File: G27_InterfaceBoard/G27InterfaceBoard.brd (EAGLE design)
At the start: 60 x 60 mm, 24 parts, among them IC1 LMV321M5, J1 Pedal, J2 Shifter, J3 Steering, U1 LMV324

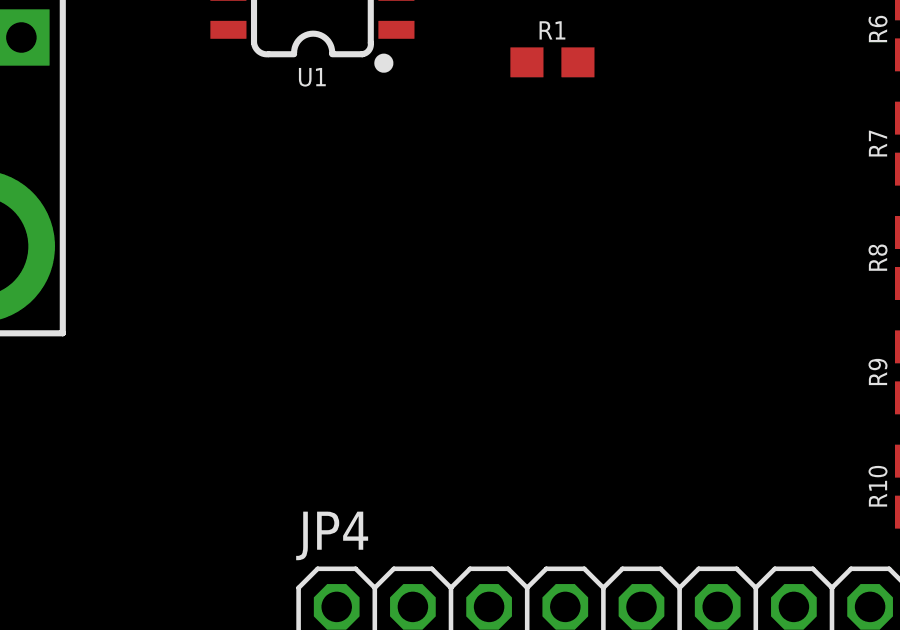
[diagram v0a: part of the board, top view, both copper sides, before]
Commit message: Modfications to board based on testing.
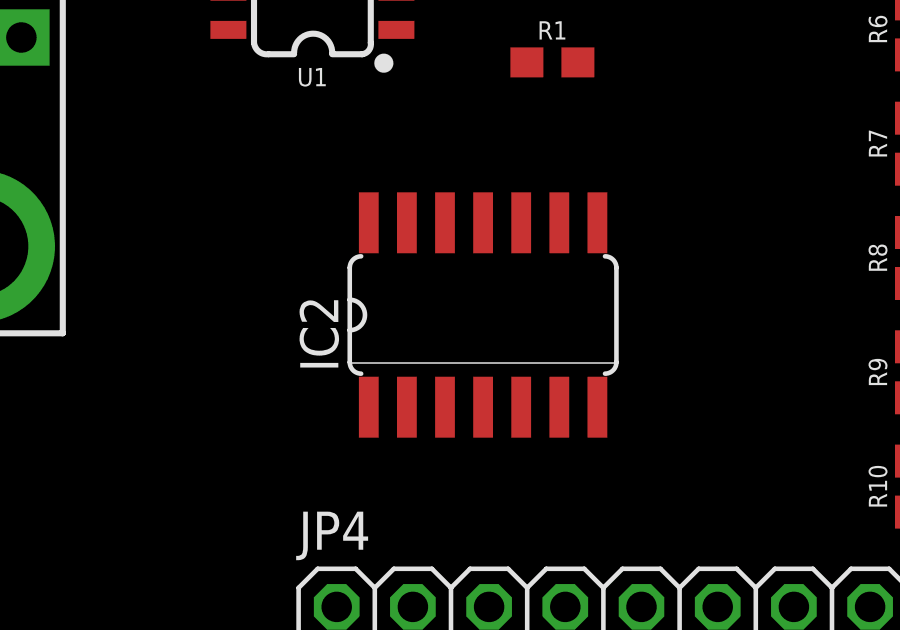
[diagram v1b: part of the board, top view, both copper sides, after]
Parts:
- added IC2: 74HC126D, 74xx-eu:SO14
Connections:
- removed net !SHIFT_CS: J2.3, JP4.17
- removed net !WBTN_CS: JP4.13
- removed net !WLED_CS: JP4.15
- removed net +5V: C1.1, C2.1, D1.3, IC1.5, J1.6, J1.9, J2.7, J2.9, J3.7, JP4.19, U1.4
- removed net N$4: C2.2, IC1.2
- new net !SHIFT_PWR_LED: J2.5
- new net SHIFT_CS: IC2.1, J2.3, JP4.17
- new net SHIFT_MISO: IC2.2, J2.2
- new net VCC: C1.1, C2.1, D1.3, IC1.5, IC2.14, J1.6, J1.9, J2.7, J2.9, J3.7, JP4.19, U1.4
- new net WMISO: IC2.5, J3.2
- net GND: now also C2.2, IC1.2, IC2.10, IC2.12, IC2.13, IC2.7, IC2.9
- net MISO: now also IC2.3, IC2.6; no longer J2.2, J3.2
- net MOSI: no longer J2.5
- net N$3: now also IC1.3; no longer IC1.1
- net SHIFT_Y: now also IC1.1; no longer IC1.3
- net WBTN_CS: now also IC2.4, JP4.13
- net WLED_LATCH: now also JP4.15
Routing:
- added copper zone on layer 1, net VCC
- removed copper zone on layer 1, net +5V
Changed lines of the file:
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@@
 <attribute name="NAME" x="48.325" y="-18.975" size="1.27" layer="25" rot="R180"/>
 <attribute name="POPULARITY" value="3" x="-12" y="35" size="1.778" layer="27" rot="R180" display="off"/>
+<attribute name="SPICEPREFIX" value="D" x="46.42" y="-17.07" size="1.778" layer="27" rot="R180" display="off"/>
 <attribute name="VALUE" x="48.325" y="-13.895" size="1.27" layer="27" rot="R180"/>
 </element>
@@
 <attribute name="VALUE" x="20.31" y="-24.97" size="0.6096" layer="27" font="vector" ratio="20" rot="R180" align="bottom-center"/>
 </element>
+<element name="IC2" library="74xx-eu" library_urn="urn:adsk.eagle:library:85" package="SO14" package3d_urn="urn:adsk.eagle:package:1010/2" value="74HC126D" x="26" y="-44" smashed="yes">
+<attribute name="NAME" x="21.174" y="-45.905" size="1.27" layer="25" ratio="10" rot="R90"/>
+<attribute name="POPULARITY" value="0" x="26" y="-44" size="1.778" layer="27" display="off"/>
+<attribute name="VALUE" x="22.825" y="-44.762" size="1.27" layer="27" ratio="10"/>
+</element>
 </elements>
 <signals>
-<signal name="+5V">
-<contactref element="J2" pad="7"/>
-<contactref element="J2" pad="9"/>
-<contactref element="JP4" pad="19"/>
-<contactref element="U1" pad="4"/>
-<contactref element="C1" pad="1"/>
-<contactref element="D1" pad="3"/>
-<contactref element="J1" pad="6"/>
-<contactref element="J1" pad="9"/>
-<contactref element="J3" pad="7"/>
-<contactref element="IC1" pad="5"/>
-<contactref element="C2" pad="1"/>
-<polygon width="0.1524" layer="1">
-<vertex x="-3" y="2"/>
-<vertex x="61" y="2"/>
-<vertex x="61" y="-62"/>
-<vertex x="-3" y="-62"/>
-</polygon>
-</signal>
 <signal name="THROTTLE">
 <contactref element="J1" pad="2"/>
@@
 <vertex x="-3" y="-61"/>
 </polygon>
-<wire x1="10.61" y1="-34.75" x2="17.51" y2="-30.685" width="0" layer="19" extent="1-1"/>
-<wire x1="40.23" y1="-50.57" x2="43.98" y2="-53.73" width="0" layer="19" extent="1-1"/>
-<wire x1="40.23" y1="-42.95" x2="45.31" y2="-47.18" width="0" layer="19" extent="1-1"/>
-<wire x1="40.23" y1="-35.33" x2="40.23" y2="-42.95" width="0" layer="19" extent="1-1"/>
-<wire x1="40.23" y1="-31.52" x2="40.23" y2="-35.33" width="0" layer="19" extent="1-1"/>
-<wire x1="40.23" y1="-27.71" x2="40.23" y2="-31.52" width="0" layer="19" extent="1-1"/>
+<contactref element="IC2" pad="7"/>
+<contactref element="IC1" pad="2"/>
+<contactref element="C2" pad="2"/>
+<contactref element="IC2" pad="12"/>
+<contactref element="IC2" pad="9"/>
+<contactref element="IC2" pad="10"/>
+<contactref element="IC2" pad="13"/>
+<wire x1="28.54" y1="-40.9266" x2="29.81" y2="-47.0734" width="0" layer="19" extent="1-1"/>
+<wire x1="27.27" y1="-40.9266" x2="28.54" y2="-40.9266" width="0" layer="19" extent="1-1"/>
+<wire x1="24.73" y1="-40.9266" x2="27.27" y2="-40.9266" width="0" layer="19" extent="1-1"/>
+<wire x1="23.46" y1="-40.9266" x2="24.73" y2="-40.9266" width="0" layer="19" extent="1-1"/>
+<wire x1="10.61" y1="-34.75" x2="28.54" y2="-40.9266" width="0" layer="19" extent="1-1"/>
+<wire x1="17.51" y1="-30.685" x2="10.61" y2="-34.75" width="0" layer="19" extent="1-1"/>
 <wire x1="27.32" y1="-30.58" x2="17.51" y2="-30.685" width="0" layer="19" extent="1-1"/>
+<wire x1="30.97" y1="-22.58" x2="27.32" y2="-30.58" width="0" layer="19" extent="1-1"/>
+<wire x1="24.47" y1="-19.446" x2="30.97" y2="-22.58" width="0" layer="19" extent="1-1"/>
+<wire x1="40.23" y1="-27.71" x2="30.97" y2="-22.58" width="0" layer="19" extent="1-1"/>
+<wire x1="40.23" y1="-31.52" x2="40.23" y2="-27.71" width="0" layer="19" extent="1-1"/>
+<wire x1="40.23" y1="-35.33" x2="40.23" y2="-31.52" width="0" layer="19" extent="1-1"/>
+<wire x1="40.23" y1="-42.95" x2="40.23" y2="-35.33" width="0" layer="19" extent="1-1"/>
+<wire x1="45.31" y1="-47.18" x2="40.23" y2="-42.95" width="0" layer="19" extent="1-1"/>
+<wire x1="40.23" y1="-50.57" x2="45.31" y2="-47.18" width="0" layer="19" extent="1-1"/>
+<wire x1="43.98" y1="-53.73" x2="40.23" y2="-50.57" width="0" layer="19" extent="1-1"/>
+<wire x1="34.94" y1="-7.72" x2="30.97" y2="-22.58" width="0" layer="19" extent="1-1"/>
 </signal>
 <signal name="SCK">
@@
 </signal>
 <signal name="MISO">
-<contactref element="J2" pad="2"/>
 <contactref element="JP4" pad="16"/>
-<contactref element="J3" pad="2"/>
-<wire x1="45.31" y1="-44.64" x2="33.56" y2="-10.56" width="0" layer="19" extent="1-1"/>
-<wire x1="38.9" y1="-53.73" x2="45.31" y2="-44.64" width="0" layer="19" extent="1-1"/>
-</signal>
-<signal name="!SHIFT_CS">
+<contactref element="IC2" pad="3"/>
+<contactref element="IC2" pad="6"/>
+<wire x1="28.54" y1="-47.0734" x2="24.73" y2="-47.0734" width="0" layer="19" extent="1-1"/>
+<wire x1="38.9" y1="-53.73" x2="28.54" y2="-47.0734" width="0" layer="19" extent="1-1"/>
+</signal>
+<signal name="SHIFT_CS">
 <contactref element="J2" pad="3"/>
 <contactref element="JP4" pad="17"/>
-<wire x1="41.44" y1="-56.27" x2="30.79" y2="-10.56" width="0" layer="19" extent="1-1"/>
+<contactref element="IC2" pad="1"/>
+<wire x1="41.44" y1="-56.27" x2="22.19" y2="-47.0734" width="0" layer="19" extent="1-1"/>
+<wire x1="30.79" y1="-10.56" x2="41.44" y2="-56.27" width="0" layer="19" extent="1-1"/>
 </signal>
 <signal name="SHIFT_X">
@@
 </signal>
 <signal name="MOSI">
-<contactref element="J2" pad="5"/>
 <contactref element="JP4" pad="14"/>
 <contactref element="J3" pad="3"/>
 <wire x1="45.31" y1="-42.1" x2="36.36" y2="-53.73" width="0" layer="19" extent="1-1"/>
-<wire x1="25.25" y1="-10.56" x2="45.31" y2="-42.1" width="0" layer="19" extent="1-1"/>
 </signal>
 <signal name="SHIFT_Y">
 <contactref element="J2" pad="8"/>
-<contactref element="IC1" pad="3"/>
-<wire x1="25.42" y1="-19.446" x2="29.41" y2="-7.72" width="0" layer="19" extent="1-1"/>
-</signal>
-<signal name="!WLED_CS">
-<contactref element="JP4" pad="15"/>
-</signal>
-<signal name="!WBTN_CS">
-<contactref element="JP4" pad="13"/>
+<contactref element="IC1" pad="1"/>
+<wire x1="23.52" y1="-19.446" x2="29.41" y2="-7.72" width="0" layer="19" extent="1-1"/>
 </signal>
 <signal name="N$1">
@@
 <signal name="WLED_LATCH">
 <contactref element="J3" pad="5"/>
+<contactref element="JP4" pad="15"/>
+<wire x1="45.31" y1="-37.02" x2="38.9" y2="-56.27" width="0" layer="19" extent="1-1"/>
 </signal>
 <signal name="WBTN_CS">
 <contactref element="J3" pad="6"/>
+<contactref element="JP4" pad="13"/>
+<contactref element="IC2" pad="4"/>
+<wire x1="36.36" y1="-56.27" x2="26" y2="-47.0734" width="0" layer="19" extent="1-1"/>
+<wire x1="45.31" y1="-34.48" x2="36.36" y2="-56.27" width="0" layer="19" extent="1-1"/>
 </signal>
 <signal name="N$2">
@@
 <wire x1="40.23" y1="-41.25" x2="40.23" y2="-37.44" width="0" layer="19" extent="1-1"/>
 </signal>
-<signal name="N$4">
-<contactref element="IC1" pad="2"/>
-<contactref element="C2" pad="2"/>
-<wire x1="24.47" y1="-19.446" x2="30.97" y2="-22.58" width="0" layer="19" extent="1-1"/>
-</signal>
 <signal name="N$3">
-<contactref element="IC1" pad="1"/>
 <contactref element="IC1" pad="4"/>
 <contactref element="R9" pad="1"/>
-<wire x1="23.52" y1="-19.446" x2="25.42" y2="-16.834" width="0" layer="19" extent="1-1"/>
-<wire x1="40.23" y1="-46.76" x2="23.52" y2="-19.446" width="0" layer="19" extent="1-1"/>
+<contactref element="IC1" pad="3"/>
+<wire x1="25.42" y1="-19.446" x2="25.42" y2="-16.834" width="0" layer="19" extent="1-1"/>
+<wire x1="40.23" y1="-46.76" x2="25.42" y2="-19.446" width="0" layer="19" extent="1-1"/>
 </signal>
 <signal name="SHIFT_Y_3_3">
@@
 <wire x1="40.23" y1="-48.87" x2="40.23" y2="-45.06" width="0" layer="19" extent="1-1"/>
 </signal>
+<signal name="!SHIFT_PWR_LED">
+<contactref element="J2" pad="5"/>
+</signal>
+<signal name="VCC">
+<contactref element="IC2" pad="14"/>
+<contactref element="JP4" pad="19"/>
+<contactref element="J2" pad="7"/>
+<contactref element="J2" pad="9"/>
+<contactref element="U1" pad="4"/>
+<contactref element="C1" pad="1"/>
+<contactref element="D1" pad="3"/>
+<contactref element="J1" pad="6"/>
+<contactref element="J1" pad="9"/>
+<contactref element="J3" pad="7"/>
+<contactref element="IC1" pad="5"/>
+<contactref element="C2" pad="1"/>
+<polygon width="0.1524" layer="1">
+<vertex x="-3" y="2"/>
+<vertex x="61" y="2"/>
+<vertex x="61" y="-62"/>
+<vertex x="-3" y="-62"/>
+</polygon>
+<wire x1="7.77" y1="-33.36" x2="22.19" y2="-40.9266" width="0" layer="19" extent="1-1"/>
+<wire x1="7.77" y1="-25.06" x2="7.77" y2="-33.36" width="0" layer="19" extent="1-1"/>
+<wire x1="23.11" y1="-30.685" x2="7.77" y2="-33.36" width="0" layer="19" extent="1-1"/>
+<wire x1="25.62" y1="-30.58" x2="23.11" y2="-30.685" width="0" layer="19" extent="1-1"/>
+<wire x1="29.27" y1="-22.58" x2="25.62" y2="-30.58" width="0" layer="19" extent="1-1"/>
+<wire x1="23.52" y1="-16.834" x2="29.27" y2="-22.58" width="0" layer="19" extent="1-1"/>
+<wire x1="26.64" y1="-7.72" x2="23.52" y2="-16.834" width="0" layer="19" extent="1-1"/>
+<wire x1="32.17" y1="-7.72" x2="26.64" y2="-7.72" width="0" layer="19" extent="1-1"/>
+<wire x1="46.42" y1="-18.17" x2="32.17" y2="-7.72" width="0" layer="19" extent="1-1"/>
+<wire x1="45.31" y1="-31.94" x2="46.42" y2="-18.17" width="0" layer="19" extent="1-1"/>
+<wire x1="43.98" y1="-56.27" x2="45.31" y2="-31.94" width="0" layer="19" extent="1-1"/>
+</signal>
+<signal name="WMISO">
+<contactref element="J3" pad="2"/>
+<contactref element="IC2" pad="5"/>
+<wire x1="45.31" y1="-44.64" x2="27.27" y2="-47.0734" width="0" layer="19" extent="1-1"/>
+</signal>
+<signal name="SHIFT_MISO">
+<contactref element="J2" pad="2"/>
+<contactref element="IC2" pad="2"/>
+<wire x1="33.56" y1="-10.56" x2="23.46" y2="-47.0734" width="0" layer="19" extent="1-1"/>
+</signal>
 </signals>

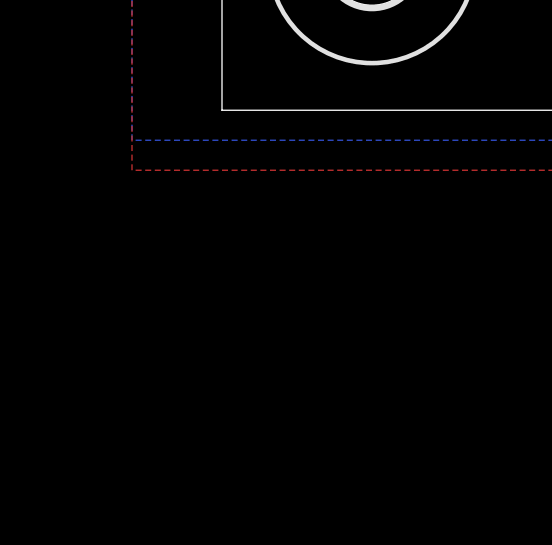
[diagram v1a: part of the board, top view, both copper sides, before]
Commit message: Add some termination resistors to the SPI lines.
A breadboarded version of this is now working with the G27 shifter
and wheel simulataneously. LED control is not yet tested.
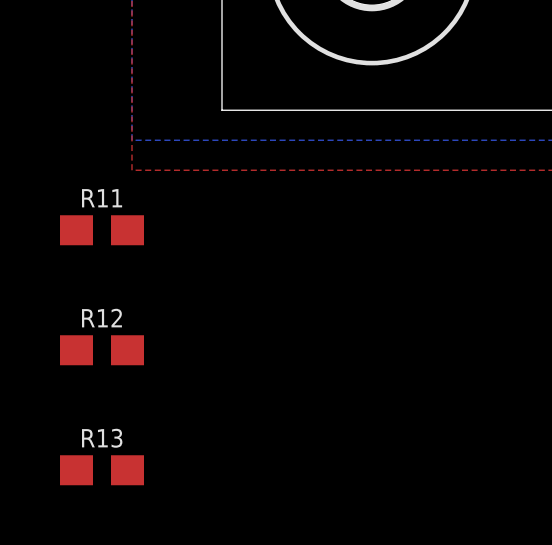
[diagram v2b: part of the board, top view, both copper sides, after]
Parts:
- added R11, R12: 50, SparkFun-Resistors:0603
- added R13: 100, SparkFun-Resistors:0603
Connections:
- new net N$4: JP4.18, R11.1
- new net N$7: JP4.14, R12.1
- new net N$8: J3.2, R13.1
- net MOSI: now also R12.2; no longer JP4.14
- net SCK: now also R11.2; no longer JP4.18
- net WMISO: now also R13.2; no longer J3.2
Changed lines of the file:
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@@
 <attribute name="VALUE" x="22.825" y="-44.762" size="1.27" layer="27" ratio="10"/>
+</element>
+<element name="R11" library="SparkFun-Resistors" library_urn="urn:adsk.eagle:library:532" package="0603" package3d_urn="urn:adsk.eagle:package:39650/1" value="50" x="-4" y="-64" smashed="yes">
+<attribute name="NAME" x="-4" y="-63.238" size="0.6096" layer="25" font="vector" ratio="20" align="bottom-center"/>
+<attribute name="PROD_ID" value=" " x="-4" y="-64" size="1.778" layer="27" display="off"/>
+<attribute name="VALUE" x="-4" y="-64.762" size="0.6096" layer="27" font="vector" ratio="20" align="top-center"/>
+</element>
+<element name="R12" library="SparkFun-Resistors" library_urn="urn:adsk.eagle:library:532" package="0603" package3d_urn="urn:adsk.eagle:package:39650/1" value="50" x="-4" y="-68" smashed="yes">
+<attribute name="NAME" x="-4" y="-67.238" size="0.6096" layer="25" font="vector" ratio="20" align="bottom-center"/>
+<attribute name="PROD_ID" value=" " x="-4" y="-68" size="1.778" layer="27" display="off"/>
+<attribute name="VALUE" x="-4" y="-68.762" size="0.6096" layer="27" font="vector" ratio="20" align="top-center"/>
+</element>
+<element name="R13" library="SparkFun-Resistors" library_urn="urn:adsk.eagle:library:532" package="0603" package3d_urn="urn:adsk.eagle:package:39650/1" value="100" x="-4" y="-72" smashed="yes">
+<attribute name="NAME" x="-4" y="-71.238" size="0.6096" layer="25" font="vector" ratio="20" align="bottom-center"/>
+<attribute name="PROD_ID" value=" " x="-4" y="-72" size="1.778" layer="27" display="off"/>
+<attribute name="VALUE" x="-4" y="-72.762" size="0.6096" layer="27" font="vector" ratio="20" align="top-center"/>
 </element>
 </elements>
@@
 <signal name="SCK">
 <contactref element="J2" pad="1"/>
-<contactref element="JP4" pad="18"/>
 <contactref element="J3" pad="4"/>
-<wire x1="45.31" y1="-39.56" x2="36.33" y2="-10.56" width="0" layer="19" extent="1-1"/>
-<wire x1="41.44" y1="-53.73" x2="45.31" y2="-39.56" width="0" layer="19" extent="1-1"/>
+<contactref element="R11" pad="2"/>
+<wire x1="45.31" y1="-39.56" x2="-3.15" y2="-64" width="0" layer="19" extent="1-1"/>
+<wire x1="36.33" y1="-10.56" x2="45.31" y2="-39.56" width="0" layer="19" extent="1-1"/>
 </signal>
 <signal name="MISO">
@@
 </signal>
 <signal name="MOSI">
-<contactref element="JP4" pad="14"/>
 <contactref element="J3" pad="3"/>
-<wire x1="45.31" y1="-42.1" x2="36.36" y2="-53.73" width="0" layer="19" extent="1-1"/>
+<contactref element="R12" pad="2"/>
+<wire x1="45.31" y1="-42.1" x2="-3.15" y2="-68" width="0" layer="19" extent="1-1"/>
 </signal>
 <signal name="SHIFT_Y">
@@
 </signal>
 <signal name="WMISO">
-<contactref element="J3" pad="2"/>
 <contactref element="IC2" pad="5"/>
-<wire x1="45.31" y1="-44.64" x2="27.27" y2="-47.0734" width="0" layer="19" extent="1-1"/>
+<contactref element="R13" pad="2"/>
+<wire x1="27.27" y1="-47.0734" x2="-3.15" y2="-72" width="0" layer="19" extent="1-1"/>
 </signal>
 <signal name="SHIFT_MISO">
@@
 <wire x1="33.56" y1="-10.56" x2="23.46" y2="-47.0734" width="0" layer="19" extent="1-1"/>
 </signal>
+<signal name="N$4">
+<contactref element="JP4" pad="18"/>
+<contactref element="R11" pad="1"/>
+<wire x1="41.44" y1="-53.73" x2="-4.85" y2="-64" width="0" layer="19" extent="1-1"/>
+</signal>
+<signal name="N$7">
+<contactref element="JP4" pad="14"/>
+<contactref element="R12" pad="1"/>
+<wire x1="36.36" y1="-53.73" x2="-4.85" y2="-68" width="0" layer="19" extent="1-1"/>
+</signal>
+<signal name="N$8">
+<contactref element="J3" pad="2"/>
+<contactref element="R13" pad="1"/>
+<wire x1="45.31" y1="-44.64" x2="-4.85" y2="-72" width="0" layer="19" extent="1-1"/>
+</signal>
 </signals>

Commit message: G27InterfaceBoard v1.0 as ordered.
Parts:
- removed J3: Steering, SparkFun-Connectors:1X07_LONGPADS
- removed JP4: (no value), stm_board_f407:PINHEAD_2X11
- removed R11, R12: 50, SparkFun-Resistors:0603
- added C3, C4: 0.1uF, resistor:C0805
- added C5, C6: 1.0uF, resistor:C0805
- added R14: 100, resistor:R0603
- added R15: 51, resistor:R0603
- added SPI2: (no value), pinhead:1X09
- added WHEEL: RJ45, SparkFun-Connectors:RJ45-8
- D1: value 3.3 -> 3
- H1, H2, H3, H4: value MOUNT-HOLE3.0 -> MOUNT-PAD-ROUND3.0; device holes:3,0 -> holes:3,0-PAD
- R1, R2, R3, R7, R9: value 1k -> 1.2k; device SparkFun-Resistors:0603 -> resistor:R0603
- R10, R4, R5, R6, R8: value 2k -> 7.5k; device SparkFun-Resistors:0603 -> resistor:R0603
- R13: value 100 -> 51; device SparkFun-Resistors:0603 -> resistor:R0603
- moved R13 55.3 mm to (8.00, -18.0)
- moved R10 36.5 mm to (34.2, -13.7)
- moved R9 33.2 mm to (31.2, -13.9)
- moved R2 30.2 mm to (23.0, -44.0)
- moved J1 30.1 mm to (30.2, -50.8), turned to 180 degrees
- moved IC2 20.6 mm to (21.0, -24.0), turned to 270 degrees
- moved R5 19.6 mm to (23.0, -40.0), turned to 270 degrees
- moved R3 19.1 mm to (27.2, -37.0)
- moved U1 15.1 mm to (30.3, -42.7), turned to 180 degrees
- moved R6 13.5 mm to (26.8, -33.5), turned to 270 degrees
- moved R4 10.2 mm to (33.1, -34.2), turned to 0 degrees
- moved C2 7.22 mm to (33.9, -16.4), turned to 180 degrees
- moved R7 7.11 mm to (36.0, -44.0)
- moved C1 6.71 mm to (29.6, -36.5), turned to 90 degrees
- moved R1 5.86 mm to (34.0, -37.0), turned to 90 degrees
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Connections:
- removed net N$4: JP4.18, R11.1
- removed net N$7: JP4.14, R12.1
- new net N$10: R15.1, SPI2.6
- new net N$9: R14.1, WHEEL.4
- new net SCLK: WHEEL.7
- net +3V3: now also C4.1, C6.1, SPI2.2
- net GND: now also C3.2, C4.2, C5.2, C6.2, H1.B3,0, H2.B3,0, H3.B3,0, H4.B3,0, SPI2.1, WHEEL.2, WHEEL.8; no longer J3.1, JP4.20
- net MISO: now also SPI2.5; no longer JP4.16
- net MOSI: now also R15.2, WHEEL.5; no longer J3.3, R12.2
- net N$8: now also SPI2.4; no longer J3.2
- net SCK: now also R13.2; no longer J3.4, R11.2
- net SHIFT_CS: now also SPI2.7; no longer JP4.17
- net VCC: now also C3.1, C5.1, SPI2.9, WHEEL.1; no longer J3.7, JP4.19
- net WBTN_CS: now also SPI2.3, WHEEL.3; no longer J3.6, JP4.13
- net WLED_LATCH: now also SPI2.8, WHEEL.6; no longer J3.5, JP4.15
- net WMISO: now also R14.2; no longer R13.2
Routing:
- net +3V3: track 0.00 -> 70.9 mm
- net SHIFT_X: track 0.00 -> 43.1 mm, vias 0 -> 1
- net GND: track 0.00 -> 42.2 mm, vias 0 -> 9
- net BRAKE_3_3: track 0.00 -> 41.1 mm, vias 0 -> 2
- net WBTN_CS: track 0.00 -> 38.6 mm, vias 0 -> 1
- net CLUTCH_3_3: track 0.00 -> 38.0 mm
- net SHIFT_CS: track 0.00 -> 33.3 mm, vias 0 -> 2
- net SCK: track 0.00 -> 32.1 mm, vias 0 -> 1
- net SHIFT_X_3_3: track 0.00 -> 29.1 mm
- net SHIFT_Y_3_3: track 0.00 -> 28.1 mm, vias 0 -> 1
- net THROTTLE_3_3: track 0.00 -> 27.1 mm
- net WLED_LATCH: track 0.00 -> 26.3 mm, vias 0 -> 3
- net MOSI: track 0.00 -> 25.1 mm, vias 0 -> 1
- net MISO: track 0.00 -> 22.4 mm
- net SHIFT_MISO: track 0.00 -> 20.1 mm, vias 0 -> 1
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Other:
- outline, holes or cut-outs redrawn
- board text added: "G27 Interface Board v1.0"
- board text added: "Pedals"
- board text added: "Shifter"
- board text added: "Wheel"
